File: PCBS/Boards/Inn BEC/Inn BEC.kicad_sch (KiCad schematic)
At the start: 6 parts, among them U1 XL1509-5.0, U2 L7805

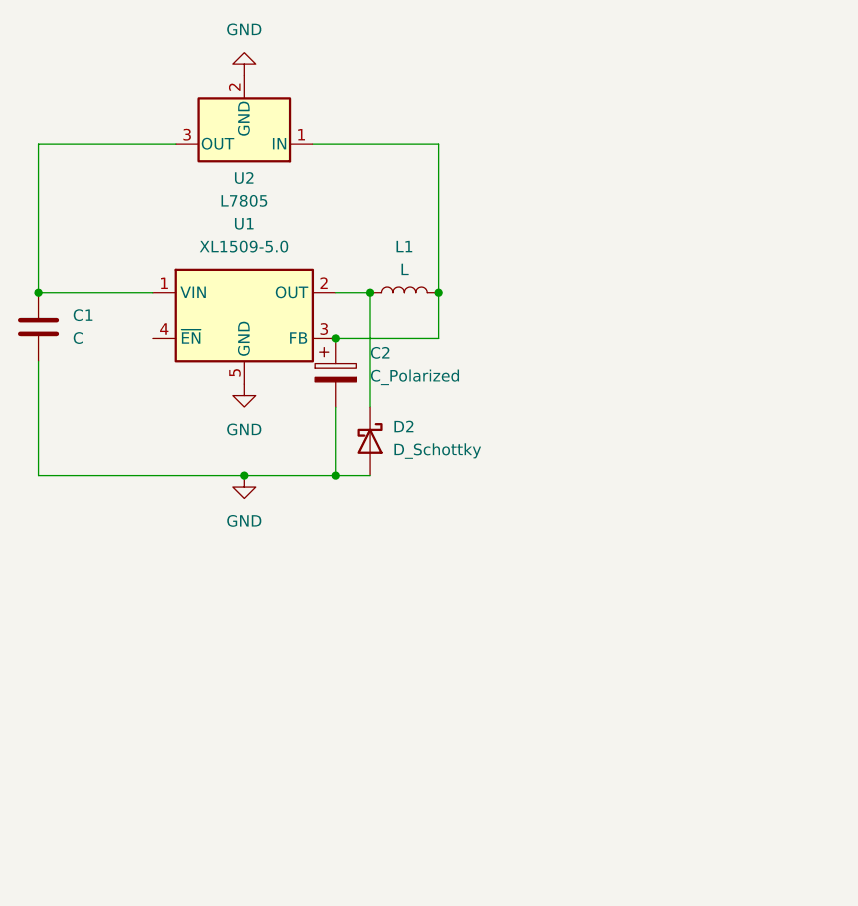
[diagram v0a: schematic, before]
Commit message: updates files for INN BEC, adds production files and panelized version
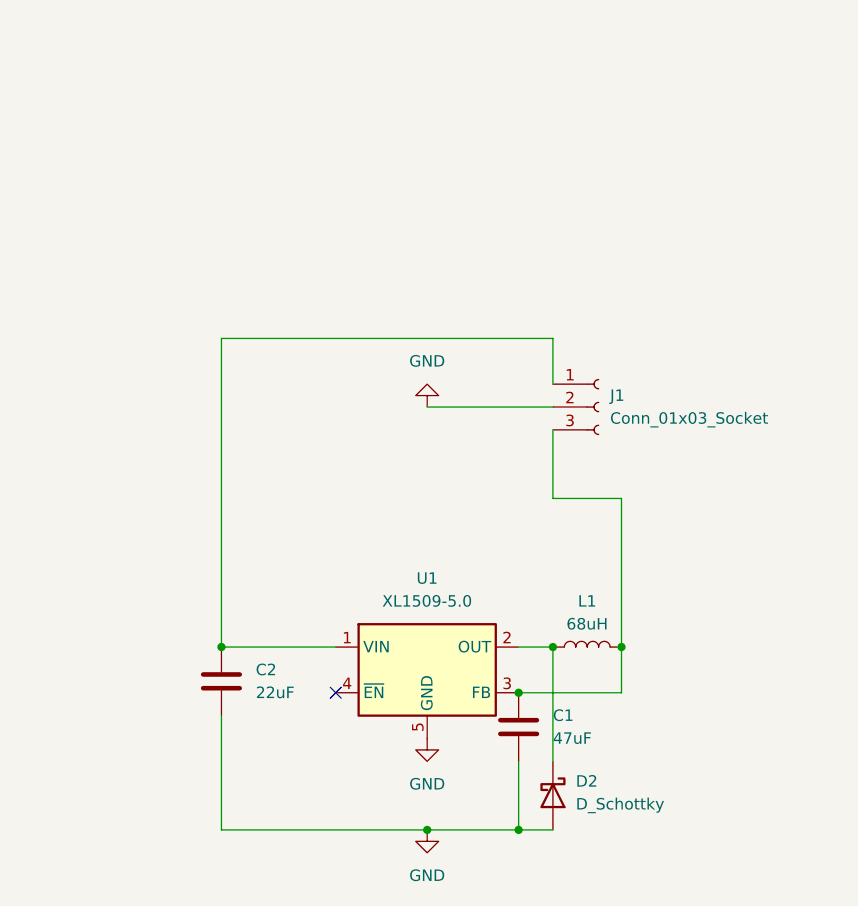
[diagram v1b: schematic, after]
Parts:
- removed C2: C_Polarized, Capacitor_SMD:CP_Elec_6.3x7.7, symbol Device:C_Polarized
- removed U2: L7805, Package_TO_SOT_SMD:TO-252-2, symbol Regulator_Linear:L7805
- added C2: 22uF, Capacitor_SMD:C_0805_2012Metric_Pad1.18x1.45mm_HandSolder, symbol Device:C
- added J1: Conn_01x03_Socket, Package_TO_SOT_SMD:TO-252-2, symbol Connector:Conn_01x03_Socket
- C1: value C -> 47uF; footprint Capacitor_SMD:C_Elec_10x10.2 -> Capacitor_SMD:C_1210_3225Metric_Pad1.33x2.70mm_HandSolder
- L1: value L -> 68uH
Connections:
- net GND: now also C2.2, J1.2 (Pin_2)
- net at L1.2, U1.3 (FB): now also C1.1, J1.3 (Pin_3)
- net at U1.1 (VIN): now also C2.1, J1.1 (Pin_1); no longer C1.1
- no-connect marks 0 -> 1
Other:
- moved on the sheet: C1, D2, L1, U1

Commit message: updated readme and PCB files
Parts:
- removed J1: Conn_01x03_Socket, Package_TO_SOT_SMD:TO-252-2, symbol Connector:Conn_01x03_Socket
- added J1, J2: Conn_01x02_Pin, Connector_Wire:SolderWire-0.1sqmm_1x02_P3.6mm_D0.4mm_OD1mm, symbol Connector:Conn_01x02_Pin
- renumbered C2 to C1, C1 to C2, D2 to D1
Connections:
- net GND: now also J1.1 (Pin_1), J2.2 (Pin_2)
- net at C1.1, U1.1 (VIN): now also J1.2 (Pin_2)
- net at C2.1, L1.2, U1.3 (FB): now also J2.1 (Pin_1)
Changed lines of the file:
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@@
+	)
+	(junction
+		(at 168.91 88.9)
+		(diameter 0)
+		(color 0 0 0 0)
 	)
 	(junction
@@
 	(wire
 		(pts
+			(xy 172.72 91.44) (xy 168.91 91.44)
+		)
+		(stroke
+			(width 0)
+			(type default)
+		)
+	)
+	(wire
+		(pts
 			(xy 151.13 128.27) (xy 161.29 128.27)
 		)
@@
 	(wire
 		(pts
-			(xy 165.1 83.82) (xy 165.1 91.44)
-		)
-		(stroke
-			(width 0)
-			(type default)
-		)
-	)
-	(wire
-		(pts
-			(xy 128.27 73.66) (xy 128.27 107.95)
-		)
-		(stroke
-			(width 0)
-			(type default)
-		)
-	)
-	(wire
-		(pts
-			(xy 165.1 73.66) (xy 128.27 73.66)
-		)
-		(stroke
-			(width 0)
-			(type default)
-		)
-	)
-	(wire
-		(pts
-			(xy 165.1 73.66) (xy 165.1 78.74)
+			(xy 128.27 83.82) (xy 128.27 107.95)
+		)
+		(stroke
+			(width 0)
+			(type default)
+		)
+	)
+	(wire
+		(pts
+			(xy 172.72 83.82) (xy 128.27 83.82)
+		)
+		(stroke
+			(width 0)
+			(type default)
+		)
+	)
+	(wire
+		(pts
+			(xy 172.72 93.98) (xy 172.72 107.95)
 		)
 		(stroke
@@
 	(wire
 		(pts
+			(xy 168.91 86.36) (xy 172.72 86.36)
+		)
+		(stroke
+			(width 0)
+			(type default)
+		)
+	)
+	(wire
+		(pts
 			(xy 128.27 115.57) (xy 128.27 128.27)
 		)
@@
 	(wire
 		(pts
-			(xy 172.72 91.44) (xy 172.72 107.95)
-		)
-		(stroke
-			(width 0)
-			(type default)
-		)
-	)
-	(wire
-		(pts
 			(xy 161.29 113.03) (xy 172.72 113.03)
 		)
@@
 	(wire
 		(pts
-			(xy 165.1 91.44) (xy 172.72 91.44)
-		)
-		(stroke
-			(width 0)
-			(type default)
-		)
-	)
-	(wire
-		(pts
 			(xy 165.1 107.95) (xy 161.29 107.95)
 		)
@@
 	(wire
 		(pts
-			(xy 151.13 81.28) (xy 165.1 81.28)
+			(xy 168.91 88.9) (xy 168.91 86.36)
+		)
+		(stroke
+			(width 0)
+			(type default)
+		)
+	)
+	(wire
+		(pts
+			(xy 166.37 88.9) (xy 168.91 88.9)
+		)
+		(stroke
+			(width 0)
+			(type default)
+		)
+	)
+	(wire
+		(pts
+			(xy 168.91 91.44) (xy 168.91 88.9)
 		)
 		(stroke
@@
 		(dnp no)
 		(fields_autoplaced yes)
-		(property "Reference" "D2"
+		(property "Reference" "D1"
 			(at 167.64 122.8724 90)
 			(effects
@@
 			(project "Inn BEC"
 				(path "/a59df22d-3377-4fdf-953a-9e124fde1686"
-					(reference "D2")
+					(reference "D1")
 					(unit 1)
 				)
@@
 	(symbol
 		(lib_id "power:GND")
-		(at 151.13 81.28 180)
-		(unit 1)
-		(exclude_from_sim no)
-		(in_bom yes)
-		(on_board yes)
-		(dnp no)
-		(fields_autoplaced yes)
-		(property "Reference" "#PWR02"
-			(at 151.13 74.93 0)
+		(at 166.37 88.9 270)
+		(unit 1)
+		(exclude_from_sim no)
+		(in_bom yes)
+		(on_board yes)
+		(dnp no)
+		(fields_autoplaced yes)
+		(property "Reference" "#PWR03"
+			(at 160.02 88.9 0)
 			(effects
 				(font
@@
 		)
 		(property "Value" "GND"
-			(at 151.13 76.2 0)
+			(at 165.1 85.09 90)
 			(effects
 				(font
@@
 		)
 		(property "Footprint" ""
-			(at 151.13 81.28 0)
+			(at 166.37 88.9 0)
 			(effects
 				(font
@@
 		)
 		(property "Datasheet" ""
-			(at 151.13 81.28 0)
+			(at 166.37 88.9 0)
 			(effects
 				(font
@@
 		)
 		(property "Description" "Power symbol creates a global label with name \"GND\" , ground"
-			(at 151.13 81.28 0)
+			(at 166.37 88.9 0)
 			(effects
 				(font
@@
 			(project "Inn BEC"
 				(path "/a59df22d-3377-4fdf-953a-9e124fde1686"
-					(reference "#PWR02")
-					(unit 1)
-				)
-			)
-		)
-	)
-	(symbol
-		(lib_id "Connector:Conn_01x03_Socket")
-		(at 170.18 81.28 0)
-		(unit 1)
-		(exclude_from_sim no)
-		(in_bom yes)
-		(on_board yes)
-		(dnp no)
-		(fields_autoplaced yes)
-		(property "Reference" "J1"
-			(at 171.45 80.0099 0)
-			(effects
-				(font
-					(size 1.27 1.27)
-				)
-				(justify left)
-			)
-		)
-		(property "Value" "Conn_01x03_Socket"
-			(at 171.45 82.5499 0)
-			(effects
-				(font
-					(size 1.27 1.27)
-				)
-				(justify left)
-			)
-		)
-		(property "Footprint" "Package_TO_SOT_SMD:TO-252-2"
-			(at 170.18 81.28 0)
+					(reference "#PWR03")
+					(unit 1)
+				)
+			)
+		)
+	)
+	(symbol
+		(lib_id "Connector:Conn_01x02_Pin")
+		(at 177.8 93.98 180)
+		(unit 1)
+		(exclude_from_sim no)
+		(in_bom yes)
+		(on_board yes)
+		(dnp no)
+		(fields_autoplaced yes)
+		(property "Reference" "J2"
+			(at 179.07 91.4399 0)
+			(effects
+				(font
+					(size 1.27 1.27)
+				)
+				(justify right)
+			)
+		)
+		(property "Value" "Conn_01x02_Pin"
+			(at 179.07 93.9799 0)
+			(effects
+				(font
+					(size 1.27 1.27)
+				)
+				(justify right)
+			)
+		)
+		(property "Footprint" "Connector_Wire:SolderWire-0.1sqmm_1x02_P3.6mm_D0.4mm_OD1mm"
+			(at 177.8 93.98 0)
 			(effects
 				(font
@@
 		)
 		(property "Datasheet" "~"
-			(at 170.18 81.28 0)
-			(effects
-				(font
-					(size 1.27 1.27)
-				)
-				(hide yes)
-			)
-		)
-		(property "Description" "Generic connector, single row, 01x03, script generated"
-			(at 170.18 81.28 0)
+			(at 177.8 93.98 0)
+			(effects
+				(font
+					(size 1.27 1.27)
+				)
+				(hide yes)
+			)
+		)
+		(property "Description" "Generic connector, single row, 01x02, script generated"
+			(at 177.8 93.98 0)
 			(effects
 				(font
@@
 		(pin "2"
 		)
-		(pin "3"
-		)
-		(pin "1"
-		)
-		(instances
-			(project ""
-				(path "/a59df22d-3377-4fdf-953a-9e124fde1686"
-					(reference "J1")
+		(pin "1"
+		)
+		(instances
+			(project "Inn BEC"
+				(path "/a59df22d-3377-4fdf-953a-9e124fde1686"
+					(reference "J2")
 					(unit 1)
 				)
@@
 		(dnp no)
 		(fields_autoplaced yes)
-		(property "Reference" "C1"
+		(property "Reference" "C2"
 			(at 165.1 115.5699 0)
 			(effects
@@
 			(project "Inn BEC"
 				(path "/a59df22d-3377-4fdf-953a-9e124fde1686"
-					(reference "C1")
+					(reference "C2")
 					(unit 1)
 				)
@@
 	)
 	(symbol
+		(lib_id "Connector:Conn_01x02_Pin")
+		(at 177.8 86.36 180)
+		(unit 1)
+		(exclude_from_sim no)
+		(in_bom yes)
+		(on_board yes)
+		(dnp no)
+		(fields_autoplaced yes)
+		(property "Reference" "J1"
+			(at 179.07 83.8199 0)
+			(effects
+				(font
+					(size 1.27 1.27)
+				)
+				(justify right)
+			)
+		)
+		(property "Value" "Conn_01x02_Pin"
+			(at 179.07 86.3599 0)
+			(effects
+				(font
+					(size 1.27 1.27)
+				)
+				(justify right)
+			)
+		)
+		(property "Footprint" "Connector_Wire:SolderWire-0.1sqmm_1x02_P3.6mm_D0.4mm_OD1mm"
+			(at 177.8 86.36 0)
+			(effects
+				(font
+					(size 1.27 1.27)
+				)
+				(hide yes)
+			)
+		)
+		(property "Datasheet" "~"
+			(at 177.8 86.36 0)
+			(effects
+				(font
+					(size 1.27 1.27)
+				)
+				(hide yes)
+			)
+		)
+		(property "Description" "Generic connector, single row, 01x02, script generated"
+			(at 177.8 86.36 0)
+			(effects
+				(font
+					(size 1.27 1.27)
+				)
+				(hide yes)
+			)
+		)
+		(pin "2"
+		)
+		(pin "1"
+		)
+		(instances
+			(project ""
+				(path "/a59df22d-3377-4fdf-953a-9e124fde1686"
+					(reference "J1")
+					(unit 1)
+				)
+			)
+		)
+	)
+	(symbol
 		(lib_id "power:GND")
 		(at 151.13 128.27 0)
@@
 		(dnp no)
 		(fields_autoplaced yes)
-		(property "Reference" "#PWR03"
+		(property "Reference" "#PWR02"
 			(at 151.13 134.62 0)
 			(effects
@@
 			(project "Inn BEC"
 				(path "/a59df22d-3377-4fdf-953a-9e124fde1686"
-					(reference "#PWR03")
+					(reference "#PWR02")
 					(unit 1)
 				)
@@
 		(dnp no)
 		(fields_autoplaced yes)
-		(property "Reference" "C2"
+		(property "Reference" "C1"
 			(at 132.08 110.4899 0)
 			(effects
@@
 			(project "Inn BEC"
 				(path "/a59df22d-3377-4fdf-953a-9e124fde1686"
-					(reference "C2")
-					(unit 1)
-				)
+					(reference "C1")
+					(unit 1)
+				)
